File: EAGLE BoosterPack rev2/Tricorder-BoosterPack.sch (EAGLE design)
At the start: 38 parts, among them U1 MAG3110, U2 LMT70LMT70, U3 HDC1000, U4 OPT3001, U5 LMP91000, U6 PGA900

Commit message: Completed PGA900 circuit, add microSD card reader
Completed PGA900 circuit, add microSD card reader
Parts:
- added C9: 0, adafruit:C-USC0603
- added U$1: MICROSD, adafruit:MICROSD
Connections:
- new net N$13: C9.2, U5.C2
- new net N$7: C9.1, U5.C1
- net 3V: now also U$1.VDD
- net GND: now also U$1.CARD_DETECT, U$1.CARD_DETECT1, U$1.GND, U$1.GND1, U$1.VSS
- net MISO: now also U$1.DATA_OUT
- net MOSI: now also U$1.DATA_IN
- net SCLK: now also U$1.SCLK
- net SD_CS: now also U$1.CS
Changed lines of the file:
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@@
 </variantdefs>
 <classes>
-<class number="0" name="default" width="0.254" drill="0.508">
+<class number="0" name="default" width="0.15" drill="0.508">
+<clearance class="0" value="0.001"/>
 </class>
 </classes>
@@
 <part name="LED3" library="adafruit" deviceset="LED" device="CHIPLED_0603"/>
 <part name="GND5" library="supply1" deviceset="GND" device=""/>
-<part name="GND6" library="supply1" deviceset="GND" device=""/>
 <part name="R6" library="resistor" deviceset="R-US_" device="R0603" value="10k"/>
 <part name="R7" library="resistor" deviceset="R-US_" device="R0603" value="10k"/>
@@
 <part name="R12" library="resistor" deviceset="R-US_" device="R0603" value="10k"/>
 <part name="JP2" library="adafruit" deviceset="PINHD-2X4" device=""/>
+<part name="C9" library="adafruit" deviceset="C-US" device="C0603" value="0"/>
+<part name="GND6" library="supply1" deviceset="GND" device=""/>
+<part name="U$1" library="adafruit" deviceset="MICROSD" device=""/>
+<part name="GND25" library="supply1" deviceset="GND" device=""/>
+<part name="GND26" library="supply1" deviceset="GND" device=""/>
+<part name="GND27" library="supply1" deviceset="GND" device=""/>
+<part name="GND28" library="supply1" deviceset="GND" device=""/>
+<part name="GND29" library="supply1" deviceset="GND" device=""/>
 </parts>
 <sheets>
 <sheet>
 <plain>
-<text x="205.74" y="139.7" size="2.54" layer="97" ratio="12">LAUNCHPAD HEADERS</text>
+<text x="160.02" y="139.7" size="2.54" layer="97" ratio="12">LAUNCHPAD HEADERS</text>
 <wire x1="2.54" y1="182.88" x2="2.54" y2="137.16" width="0.2032" layer="97" style="longdash"/>
-<wire x1="2.54" y1="137.16" x2="246.38" y2="137.16" width="0.2032" layer="97" style="longdash"/>
-<wire x1="246.38" y1="137.16" x2="246.38" y2="182.88" width="0.2032" layer="97" style="longdash"/>
+<wire x1="2.54" y1="137.16" x2="246.38" y2="139.7" width="0.2032" layer="97" style="longdash"/>
+<wire x1="246.38" y1="139.7" x2="246.38" y2="182.88" width="0.2032" layer="97" style="longdash"/>
 <wire x1="246.38" y1="182.88" x2="2.54" y2="182.88" width="0.2032" layer="97" style="longdash"/>
 </plain>
@@
 <instance part="LED3" gate="G$1" x="30.48" y="132.08" rot="R90"/>
 <instance part="GND5" gate="1" x="45.72" y="66.04" rot="R90"/>
-<instance part="GND6" gate="1" x="45.72" y="83.82" rot="R90"/>
 <instance part="R6" gate="G$1" x="35.56" y="66.04" rot="R180"/>
 <instance part="R7" gate="G$1" x="35.56" y="83.82" rot="R180"/>
@@
 <instance part="R12" gate="G$1" x="193.04" y="78.74"/>
 <instance part="JP2" gate="A" x="119.38" y="15.24"/>
+<instance part="C9" gate="G$1" x="50.8" y="53.34"/>
+<instance part="GND6" gate="1" x="45.72" y="83.82" rot="R90"/>
+<instance part="U$1" gate="G$1" x="218.44" y="170.18" rot="R90"/>
+<instance part="GND25" gate="1" x="243.84" y="147.32"/>
+<instance part="GND26" gate="1" x="238.76" y="147.32"/>
+<instance part="GND27" gate="1" x="233.68" y="147.32"/>
+<instance part="GND28" gate="1" x="198.12" y="147.32"/>
+<instance part="GND29" gate="1" x="203.2" y="147.32"/>
 </instances>
 <busses>
@@
 <label x="116.84" y="129.54" size="1.778" layer="95" rot="R90" xref="yes"/>
 </segment>
+<segment>
+<pinref part="U$1" gate="G$1" pin="VDD"/>
+<wire x1="228.6" y1="152.4" x2="228.6" y2="149.86" width="0.1524" layer="91"/>
+<label x="228.6" y="149.86" size="1.778" layer="95" rot="R270" xref="yes"/>
+</segment>
 </net>
 <net name="DC" class="0">
@@
 <label x="104.14" y="154.94" size="1.778" layer="95"/>
 </segment>
+<segment>
+<pinref part="U$1" gate="G$1" pin="SCLK"/>
+<wire x1="215.9" y1="152.4" x2="218.44" y2="149.86" width="0.1524" layer="91"/>
+<label x="218.44" y="149.86" size="1.778" layer="95" rot="R270" xref="yes"/>
+</segment>
 </net>
 <net name="SD_CS" class="0">
@@
 <label x="160.02" y="149.86" size="1.778" layer="95"/>
 </segment>
+<segment>
+<pinref part="U$1" gate="G$1" pin="CS"/>
+<wire x1="218.44" y1="152.4" x2="223.52" y2="149.86" width="0.1524" layer="91"/>
+<label x="223.52" y="149.86" size="1.778" layer="95" rot="R270" xref="yes"/>
+</segment>
 </net>
 <net name="LCD_CS" class="0">
@@
 <label x="160.02" y="154.94" size="1.778" layer="95"/>
 </segment>
+<segment>
+<pinref part="U$1" gate="G$1" pin="DATA_OUT"/>
+<wire x1="210.82" y1="152.4" x2="208.28" y2="149.86" width="0.1524" layer="91"/>
+<label x="208.28" y="149.86" size="1.778" layer="95" rot="R270" xref="yes"/>
+</segment>
 </net>
 <net name="MOSI" class="0">
@@
 <wire x1="157.48" y1="157.48" x2="160.02" y2="157.48" width="0.1524" layer="91"/>
 <label x="160.02" y="157.48" size="1.778" layer="95"/>
+</segment>
+<segment>
+<pinref part="U$1" gate="G$1" pin="DATA_IN"/>
+<wire x1="213.36" y1="152.4" x2="213.36" y2="149.86" width="0.1524" layer="91"/>
+<label x="213.36" y="149.86" size="1.778" layer="95" rot="R270" xref="yes"/>
 </segment>
 </net>
@@
 <pinref part="GND5" gate="1" pin="GND"/>
 <wire x1="40.64" y1="66.04" x2="43.18" y2="66.04" width="0.1524" layer="91"/>
-</segment>
-<segment>
-<pinref part="R7" gate="G$1" pin="1"/>
-<pinref part="GND6" gate="1" pin="GND"/>
-<wire x1="40.64" y1="83.82" x2="43.18" y2="83.82" width="0.1524" layer="91"/>
 </segment>
 <segment>
@@
 <wire x1="119.38" y1="111.76" x2="96.52" y2="111.76" width="0.1524" layer="91"/>
 <wire x1="96.52" y1="111.76" x2="96.52" y2="106.68" width="0.1524" layer="91"/>
+</segment>
+<segment>
+<pinref part="R7" gate="G$1" pin="1"/>
+<wire x1="40.64" y1="83.82" x2="43.18" y2="83.82" width="0.1524" layer="91"/>
+<pinref part="GND6" gate="1" pin="GND"/>
+</segment>
+<segment>
+<pinref part="GND27" gate="1" pin="GND"/>
+<pinref part="U$1" gate="G$1" pin="VSS"/>
+<wire x1="233.68" y1="149.86" x2="231.14" y2="149.86" width="0.1524" layer="91"/>
+<wire x1="231.14" y1="149.86" x2="231.14" y2="152.4" width="0.1524" layer="91"/>
+</segment>
+<segment>
+<pinref part="GND26" gate="1" pin="GND"/>
+<pinref part="U$1" gate="G$1" pin="GND1"/>
+<wire x1="238.76" y1="149.86" x2="236.22" y2="149.86" width="0.1524" layer="91"/>
+<wire x1="236.22" y1="149.86" x2="236.22" y2="152.4" width="0.1524" layer="91"/>
+</segment>
+<segment>
+<pinref part="GND25" gate="1" pin="GND"/>
+<pinref part="U$1" gate="G$1" pin="GND"/>
+<wire x1="243.84" y1="149.86" x2="238.76" y2="152.4" width="0.1524" layer="91"/>
+</segment>
+<segment>
+<pinref part="U$1" gate="G$1" pin="CARD_DETECT1"/>
+<pinref part="GND29" gate="1" pin="GND"/>
+<wire x1="203.2" y1="152.4" x2="203.2" y2="149.86" width="0.1524" layer="91"/>
+</segment>
+<segment>
+<pinref part="U$1" gate="G$1" pin="CARD_DETECT"/>
+<pinref part="GND28" gate="1" pin="GND"/>
+<wire x1="200.66" y1="152.4" x2="198.12" y2="149.86" width="0.1524" layer="91"/>
 </segment>
 </net>
@@
 </segment>
 </net>
+<net name="N$7" class="0">
+<segment>
+<pinref part="C9" gate="G$1" pin="1"/>
+<wire x1="50.8" y1="55.88" x2="50.8" y2="66.04" width="0.1524" layer="91"/>
+<pinref part="U5" gate="G$1" pin="C1"/>
+<wire x1="50.8" y1="66.04" x2="58.42" y2="66.04" width="0.1524" layer="91"/>
+</segment>
+</net>
+<net name="N$13" class="0">
+<segment>
+<pinref part="U5" gate="G$1" pin="C2"/>
+<wire x1="58.42" y1="60.96" x2="55.88" y2="60.96" width="0.1524" layer="91"/>
+<wire x1="55.88" y1="60.96" x2="55.88" y2="45.72" width="0.1524" layer="91"/>
+<pinref part="C9" gate="G$1" pin="2"/>
+<wire x1="55.88" y1="45.72" x2="50.8" y2="45.72" width="0.1524" layer="91"/>
+<wire x1="50.8" y1="45.72" x2="50.8" y2="48.26" width="0.1524" layer="91"/>
+</segment>
+</net>

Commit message: Hardware Design Lock
Short of finding any showstopper bugs, the hardware design and BOM is
locked.
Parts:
- C1: value (none) -> 0
- renumbered U$1 to U7

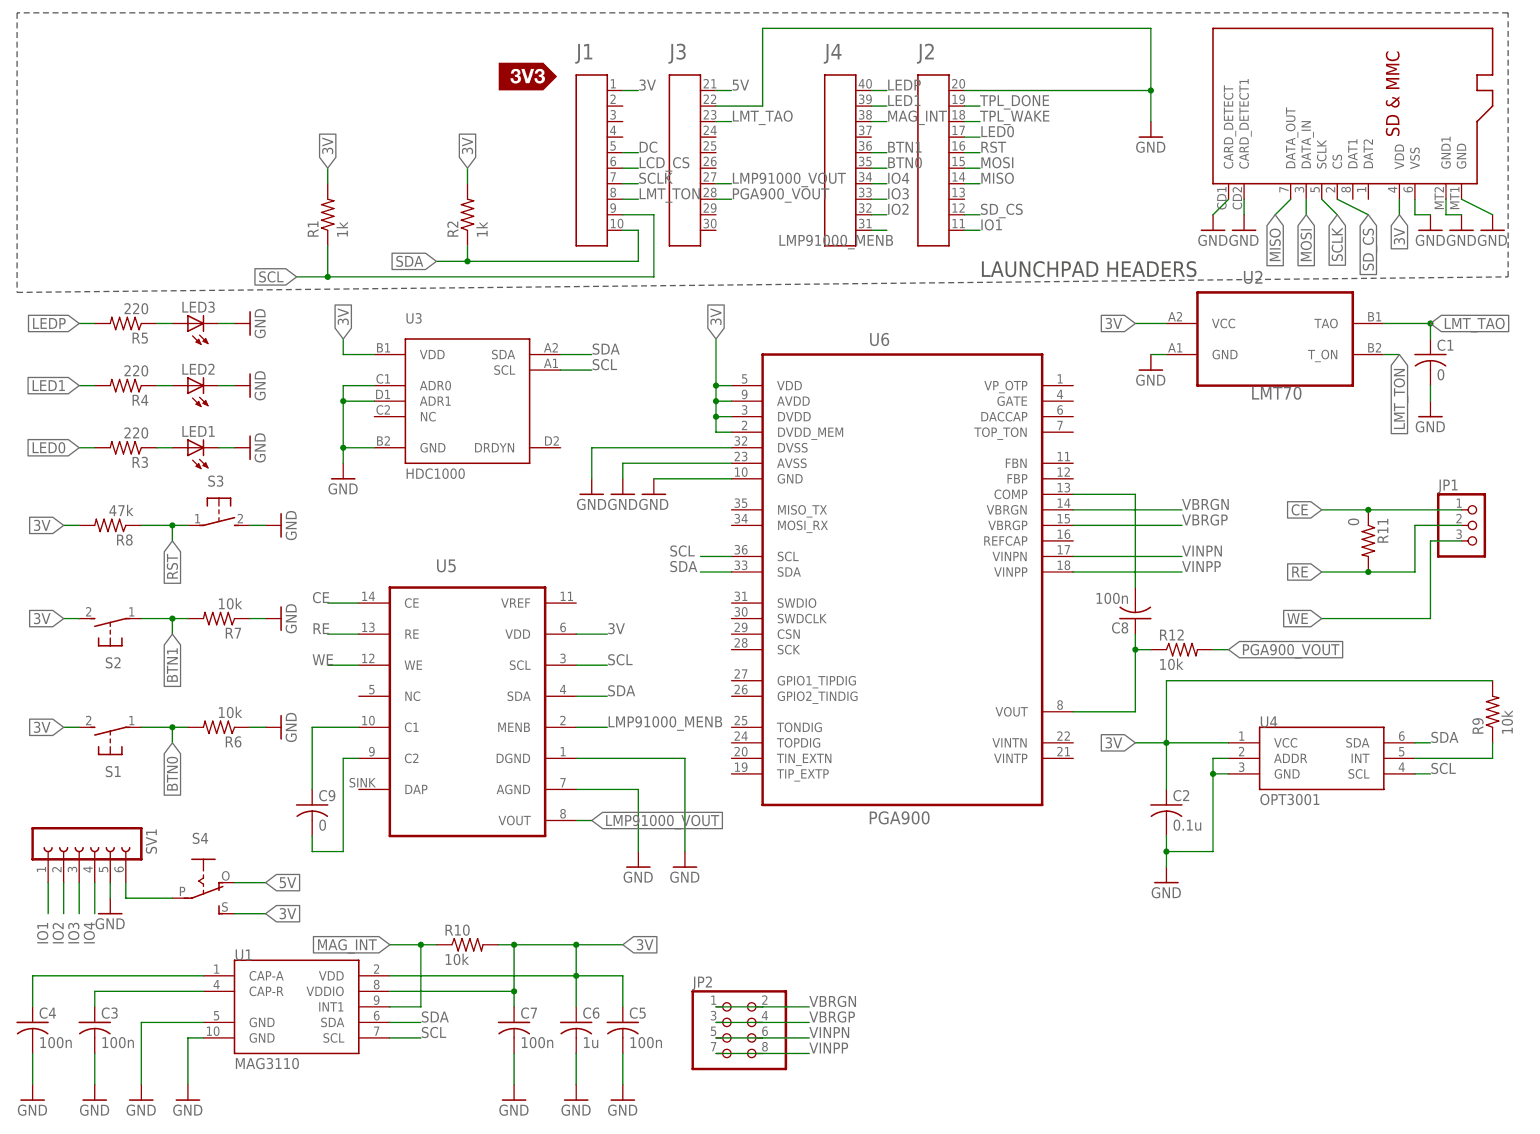
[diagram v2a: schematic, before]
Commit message: MAG3110 Circuit Fix
Removed R10, renumbered components
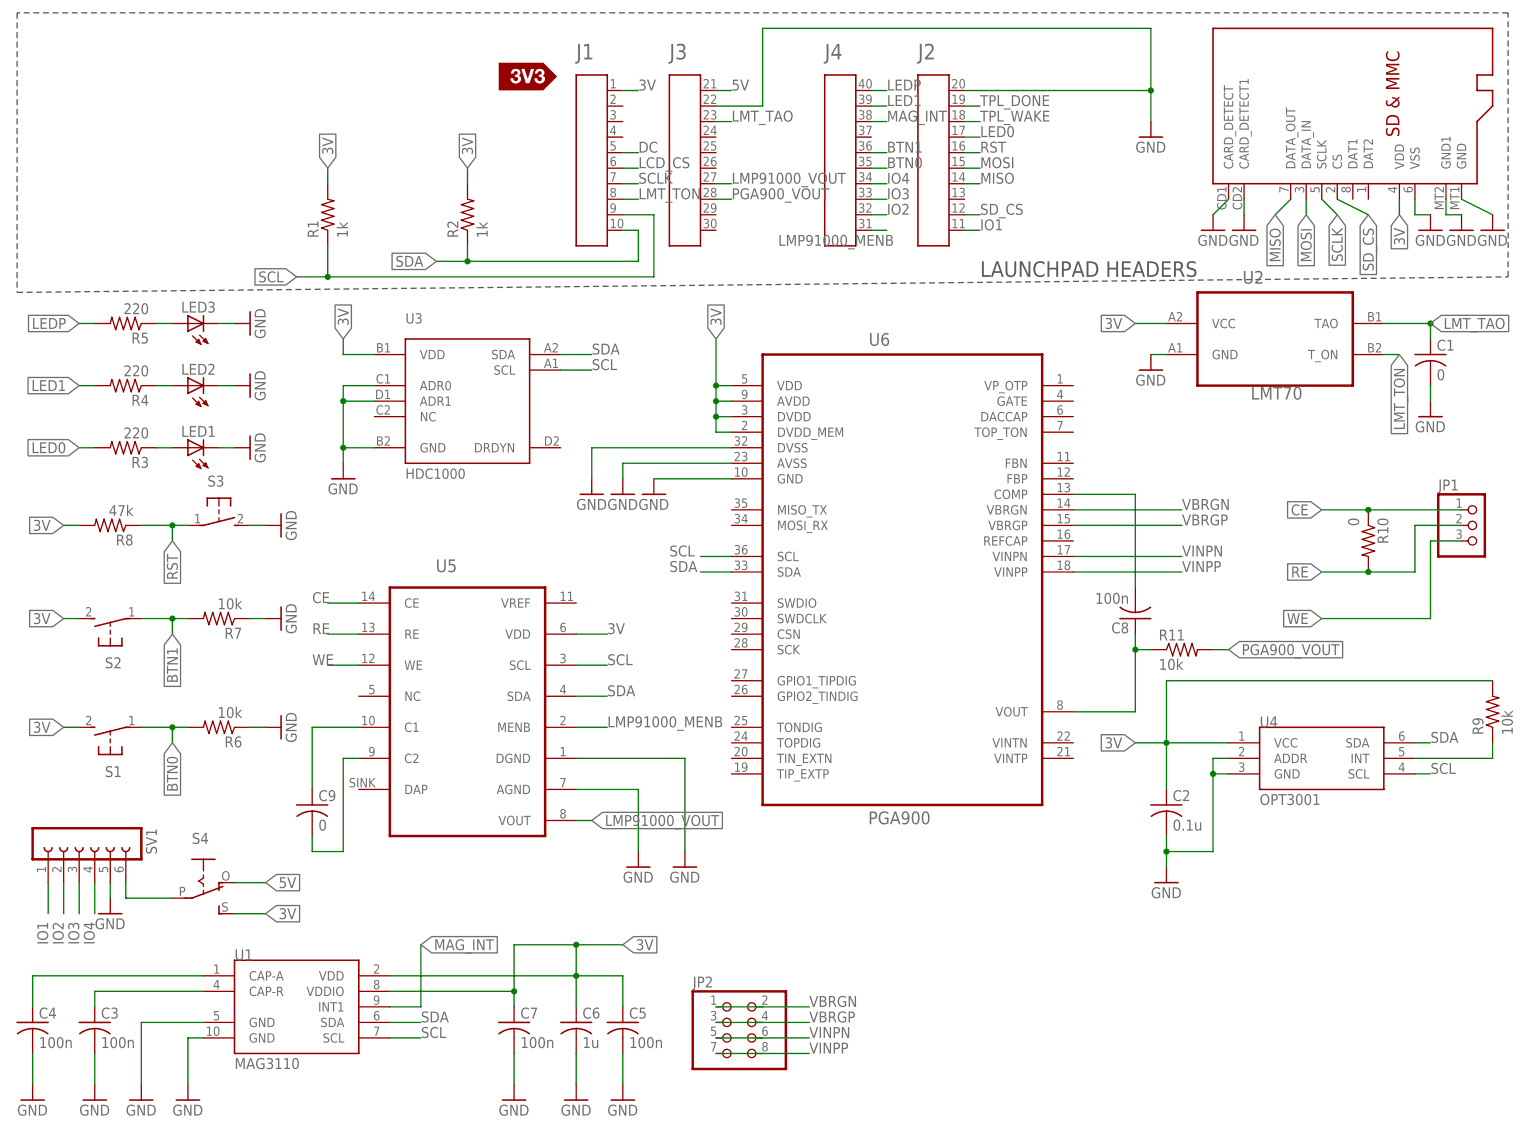
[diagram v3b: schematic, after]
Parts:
- removed R12: 10k, resistor:R-US_R0603
- R10: value 10k -> 0
- R11: value 0 -> 10k
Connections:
- removed net N$11: C5.1, C6.1, C7.1, R10.2, U1.VDD, U1.VDDIO
- net 3V: now also C5.1, C6.1, C7.1, U1.VDD, U1.VDDIO
- net CE: now also R10.1; no longer R11.1
- net MAG_INT: no longer R10.1
- net N$12: now also R11.1; no longer R12.1
- net PGA900_VOUT: now also R11.2; no longer R12.2
- net RE: now also R10.2; no longer R11.2
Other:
- moved on the sheet: R10, R11
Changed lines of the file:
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@@
 <part name="C6" library="adafruit" deviceset="C-US" device="C0603" value="1u"/>
 <part name="C7" library="adafruit" deviceset="C-US" device="C0603" value="100n"/>
-<part name="R10" library="resistor" deviceset="R-US_" device="R0603" value="10k"/>
 <part name="U5" library="LMP91000" deviceset="LMP91000" device=""/>
 <part name="GND20" library="supply1" deviceset="GND" device=""/>
 <part name="GND21" library="supply1" deviceset="GND" device=""/>
 <part name="JP1" library="adafruit" deviceset="PINHD-1X3" device="CB"/>
-<part name="R11" library="resistor" deviceset="R-US_" device="R0603" value="0"/>
+<part name="R10" library="resistor" deviceset="R-US_" device="R0603" value="0"/>
 <part name="U6" library="PGA900" deviceset="PGA900" device=""/>
 <part name="GND22" library="supply1" deviceset="GND" device=""/>
@@
 <part name="GND24" library="supply1" deviceset="GND" device=""/>
 <part name="C8" library="adafruit" deviceset="C-US" device="C0603" value="100n"/>
-<part name="R12" library="resistor" deviceset="R-US_" device="R0603" value="10k"/>
+<part name="R11" library="resistor" deviceset="R-US_" device="R0603" value="10k"/>
 <part name="JP2" library="adafruit" deviceset="PINHD-2X4" device=""/>
 <part name="C9" library="adafruit" deviceset="C-US" device="C0603" value="0"/>
@@
 <instance part="C6" gate="G$1" x="93.98" y="17.78"/>
 <instance part="C7" gate="G$1" x="83.82" y="17.78"/>
-<instance part="R10" gate="G$1" x="76.2" y="30.48"/>
 <instance part="U5" gate="G$1" x="76.2" y="78.74"/>
 <instance part="GND20" gate="1" x="111.76" y="43.18"/>
 <instance part="GND21" gate="1" x="104.14" y="43.18"/>
 <instance part="JP1" gate="A" x="241.3" y="99.06"/>
-<instance part="R11" gate="G$1" x="223.52" y="96.52" rot="R270"/>
+<instance part="R10" gate="G$1" x="223.52" y="96.52" rot="R270"/>
 <instance part="U6" gate="A" x="147.32" y="93.98"/>
 <instance part="GND22" gate="1" x="106.68" y="104.14"/>
@@
 <instance part="GND24" gate="1" x="96.52" y="104.14"/>
 <instance part="C8" gate="G$1" x="185.42" y="83.82" rot="R180"/>
-<instance part="R12" gate="G$1" x="193.04" y="78.74"/>
+<instance part="R11" gate="G$1" x="193.04" y="78.74"/>
 <instance part="JP2" gate="A" x="119.38" y="15.24"/>
 <instance part="C9" gate="G$1" x="50.8" y="53.34"/>
@@
 <wire x1="12.7" y1="83.82" x2="10.16" y2="83.82" width="0.1524" layer="91"/>
 <label x="10.16" y="83.82" size="1.778" layer="95" rot="R180" xref="yes"/>
-<label x="101.6" y="30.48" size="1.778" layer="95" xref="yes"/>
 </segment>
 <segment>
@@
 <label x="228.6" y="149.86" size="1.778" layer="95" rot="R270" xref="yes"/>
 </segment>
+<segment>
+<pinref part="U1" gate="G$1" pin="VDDIO"/>
+<pinref part="C7" gate="G$1" pin="1"/>
+<wire x1="63.5" y1="22.86" x2="83.82" y2="22.86" width="0.1524" layer="91"/>
+<wire x1="83.82" y1="22.86" x2="83.82" y2="20.32" width="0.1524" layer="91"/>
+<pinref part="U1" gate="G$1" pin="VDD"/>
+<pinref part="C5" gate="G$1" pin="1"/>
+<wire x1="63.5" y1="25.4" x2="93.98" y2="25.4" width="0.1524" layer="91"/>
+<wire x1="93.98" y1="25.4" x2="101.6" y2="25.4" width="0.1524" layer="91"/>
+<wire x1="101.6" y1="25.4" x2="101.6" y2="20.32" width="0.1524" layer="91"/>
+<pinref part="C6" gate="G$1" pin="1"/>
+<wire x1="93.98" y1="20.32" x2="93.98" y2="25.4" width="0.1524" layer="91"/>
+<wire x1="83.82" y1="30.48" x2="93.98" y2="30.48" width="0.1524" layer="91"/>
+<wire x1="93.98" y1="30.48" x2="101.6" y2="30.48" width="0.1524" layer="91"/>
+<wire x1="93.98" y1="25.4" x2="93.98" y2="30.48" width="0.1524" layer="91"/>
+<junction x="93.98" y="25.4"/>
+<junction x="93.98" y="30.48"/>
+<wire x1="83.82" y1="22.86" x2="83.82" y2="30.48" width="0.1524" layer="91"/>
+<junction x="83.82" y="22.86"/>
+<label x="101.6" y="30.48" size="1.778" layer="95" xref="yes"/>
+</segment>
 </net>
 <net name="DC" class="0">
@@
 <wire x1="63.5" y1="20.32" x2="68.58" y2="20.32" width="0.1524" layer="91"/>
 <wire x1="68.58" y1="20.32" x2="68.58" y2="30.48" width="0.1524" layer="91"/>
-<pinref part="R10" gate="G$1" pin="1"/>
-<wire x1="68.58" y1="30.48" x2="71.12" y2="30.48" width="0.1524" layer="91"/>
-<wire x1="68.58" y1="30.48" x2="63.5" y2="30.48" width="0.1524" layer="91"/>
-<junction x="68.58" y="30.48"/>
-<label x="63.5" y="30.48" size="1.778" layer="95" rot="R180" xref="yes"/>
+<label x="68.58" y="30.48" size="1.778" layer="95" xref="yes"/>
 </segment>
 </net>
@@
 </segment>
 </net>
-<net name="N$11" class="0">
-<segment>
-<pinref part="U1" gate="G$1" pin="VDDIO"/>
-<pinref part="C7" gate="G$1" pin="1"/>
-<wire x1="63.5" y1="22.86" x2="83.82" y2="22.86" width="0.1524" layer="91"/>
-<wire x1="83.82" y1="22.86" x2="83.82" y2="20.32" width="0.1524" layer="91"/>
-<pinref part="U1" gate="G$1" pin="VDD"/>
-<pinref part="C5" gate="G$1" pin="1"/>
-<wire x1="63.5" y1="25.4" x2="93.98" y2="25.4" width="0.1524" layer="91"/>
-<wire x1="93.98" y1="25.4" x2="101.6" y2="25.4" width="0.1524" layer="91"/>
-<wire x1="101.6" y1="25.4" x2="101.6" y2="20.32" width="0.1524" layer="91"/>
-<pinref part="C6" gate="G$1" pin="1"/>
-<wire x1="93.98" y1="20.32" x2="93.98" y2="25.4" width="0.1524" layer="91"/>
-<pinref part="R10" gate="G$1" pin="2"/>
-<wire x1="81.28" y1="30.48" x2="83.82" y2="30.48" width="0.1524" layer="91"/>
-<wire x1="83.82" y1="30.48" x2="93.98" y2="30.48" width="0.1524" layer="91"/>
-<wire x1="93.98" y1="30.48" x2="101.6" y2="30.48" width="0.1524" layer="91"/>
-<wire x1="93.98" y1="25.4" x2="93.98" y2="30.48" width="0.1524" layer="91"/>
-<junction x="93.98" y="25.4"/>
-<junction x="93.98" y="30.48"/>
-<wire x1="83.82" y1="22.86" x2="83.82" y2="30.48" width="0.1524" layer="91"/>
-<junction x="83.82" y="30.48"/>
-<junction x="83.82" y="22.86"/>
-</segment>
-</net>
 <net name="LMP91000_MENB" class="0">
 <segment>
@@
 <pinref part="JP1" gate="A" pin="1"/>
 <wire x1="238.76" y1="101.6" x2="223.52" y2="101.6" width="0.1524" layer="91"/>
-<pinref part="R11" gate="G$1" pin="1"/>
+<pinref part="R10" gate="G$1" pin="1"/>
 <wire x1="223.52" y1="101.6" x2="215.9" y2="101.6" width="0.1524" layer="91"/>
 <label x="215.9" y="101.6" size="1.778" layer="95" rot="R180" xref="yes"/>
@@
 <wire x1="231.14" y1="99.06" x2="231.14" y2="91.44" width="0.1524" layer="91"/>
 <wire x1="231.14" y1="91.44" x2="223.52" y2="91.44" width="0.1524" layer="91"/>
-<pinref part="R11" gate="G$1" pin="2"/>
+<pinref part="R10" gate="G$1" pin="2"/>
 <wire x1="223.52" y1="91.44" x2="215.9" y2="91.44" width="0.1524" layer="91"/>
 <label x="215.9" y="91.44" size="1.778" layer="95" rot="R180" xref="yes"/>
@@
 <wire x1="175.26" y1="68.58" x2="185.42" y2="68.58" width="0.1524" layer="91"/>
 <wire x1="185.42" y1="68.58" x2="185.42" y2="78.74" width="0.1524" layer="91"/>
-<pinref part="R12" gate="G$1" pin="1"/>
+<pinref part="R11" gate="G$1" pin="1"/>
 <wire x1="185.42" y1="78.74" x2="185.42" y2="81.28" width="0.1524" layer="91"/>
 <wire x1="187.96" y1="78.74" x2="185.42" y2="78.74" width="0.1524" layer="91"/>
@@
 </segment>
 <segment>
-<pinref part="R12" gate="G$1" pin="2"/>
+<pinref part="R11" gate="G$1" pin="2"/>
 <wire x1="198.12" y1="78.74" x2="200.66" y2="78.74" width="0.1524" layer="91"/>
 <label x="200.66" y="78.74" size="1.778" layer="95" xref="yes"/>
